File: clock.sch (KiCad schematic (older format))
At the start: 24 parts

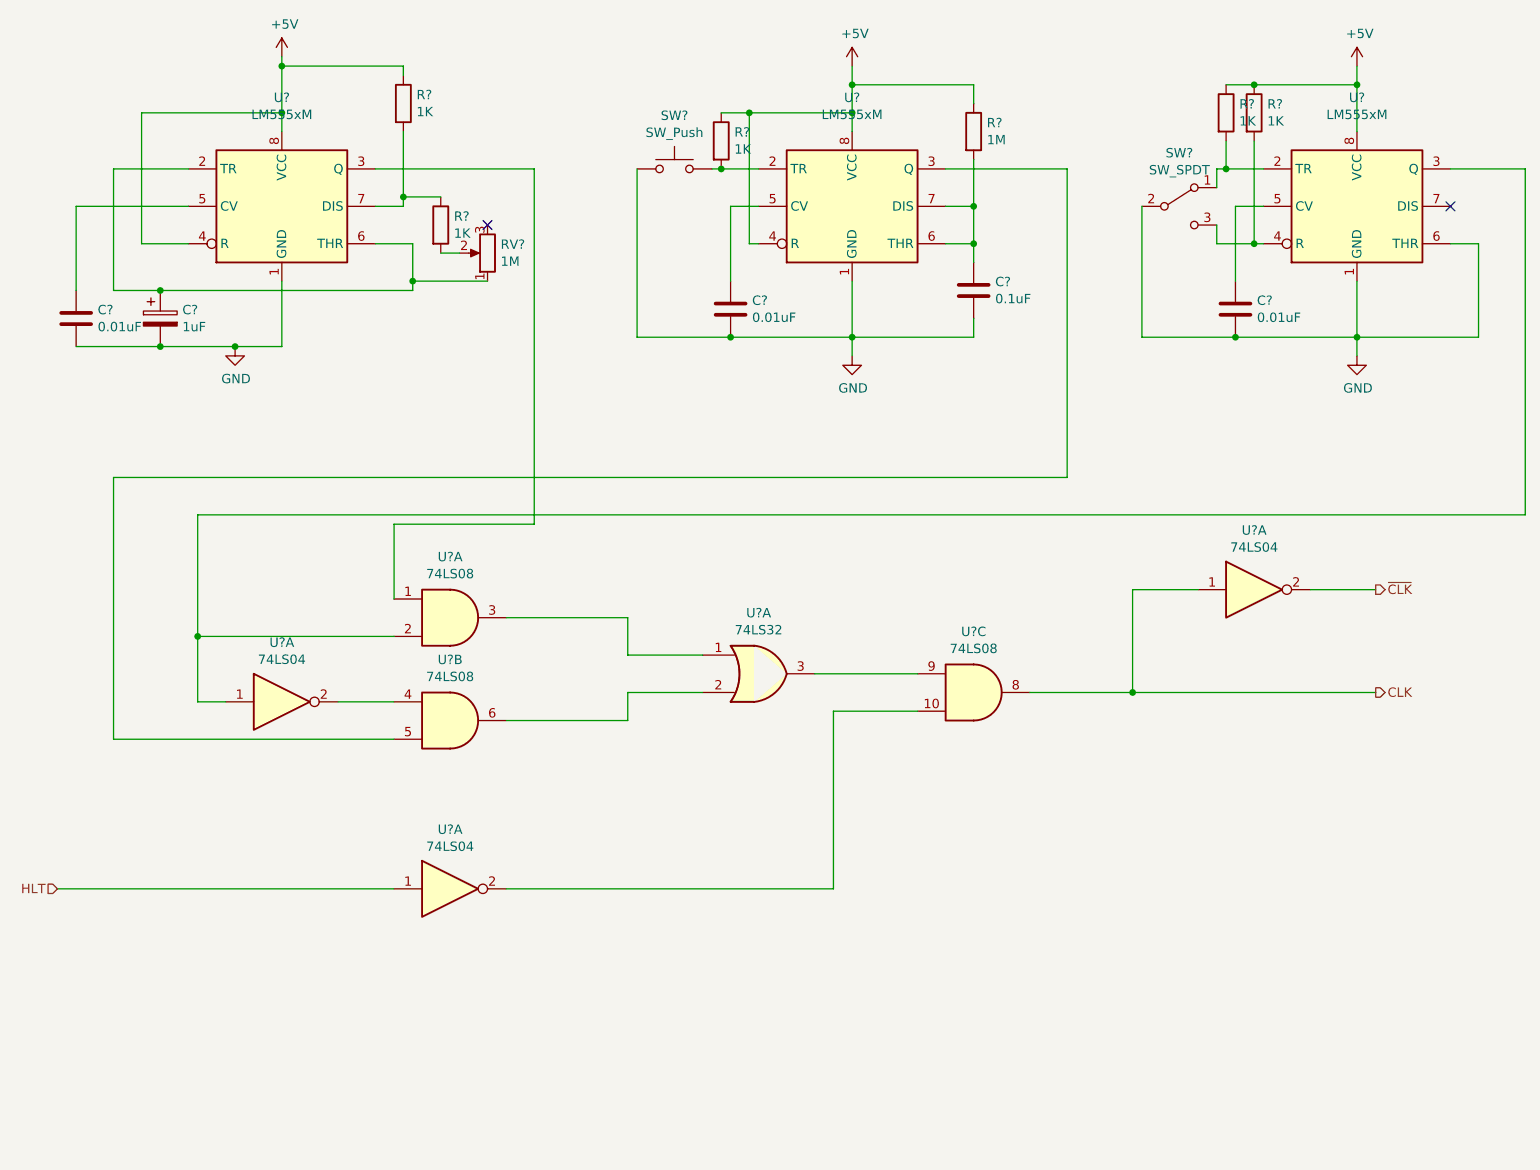
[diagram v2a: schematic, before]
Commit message: Added footprints
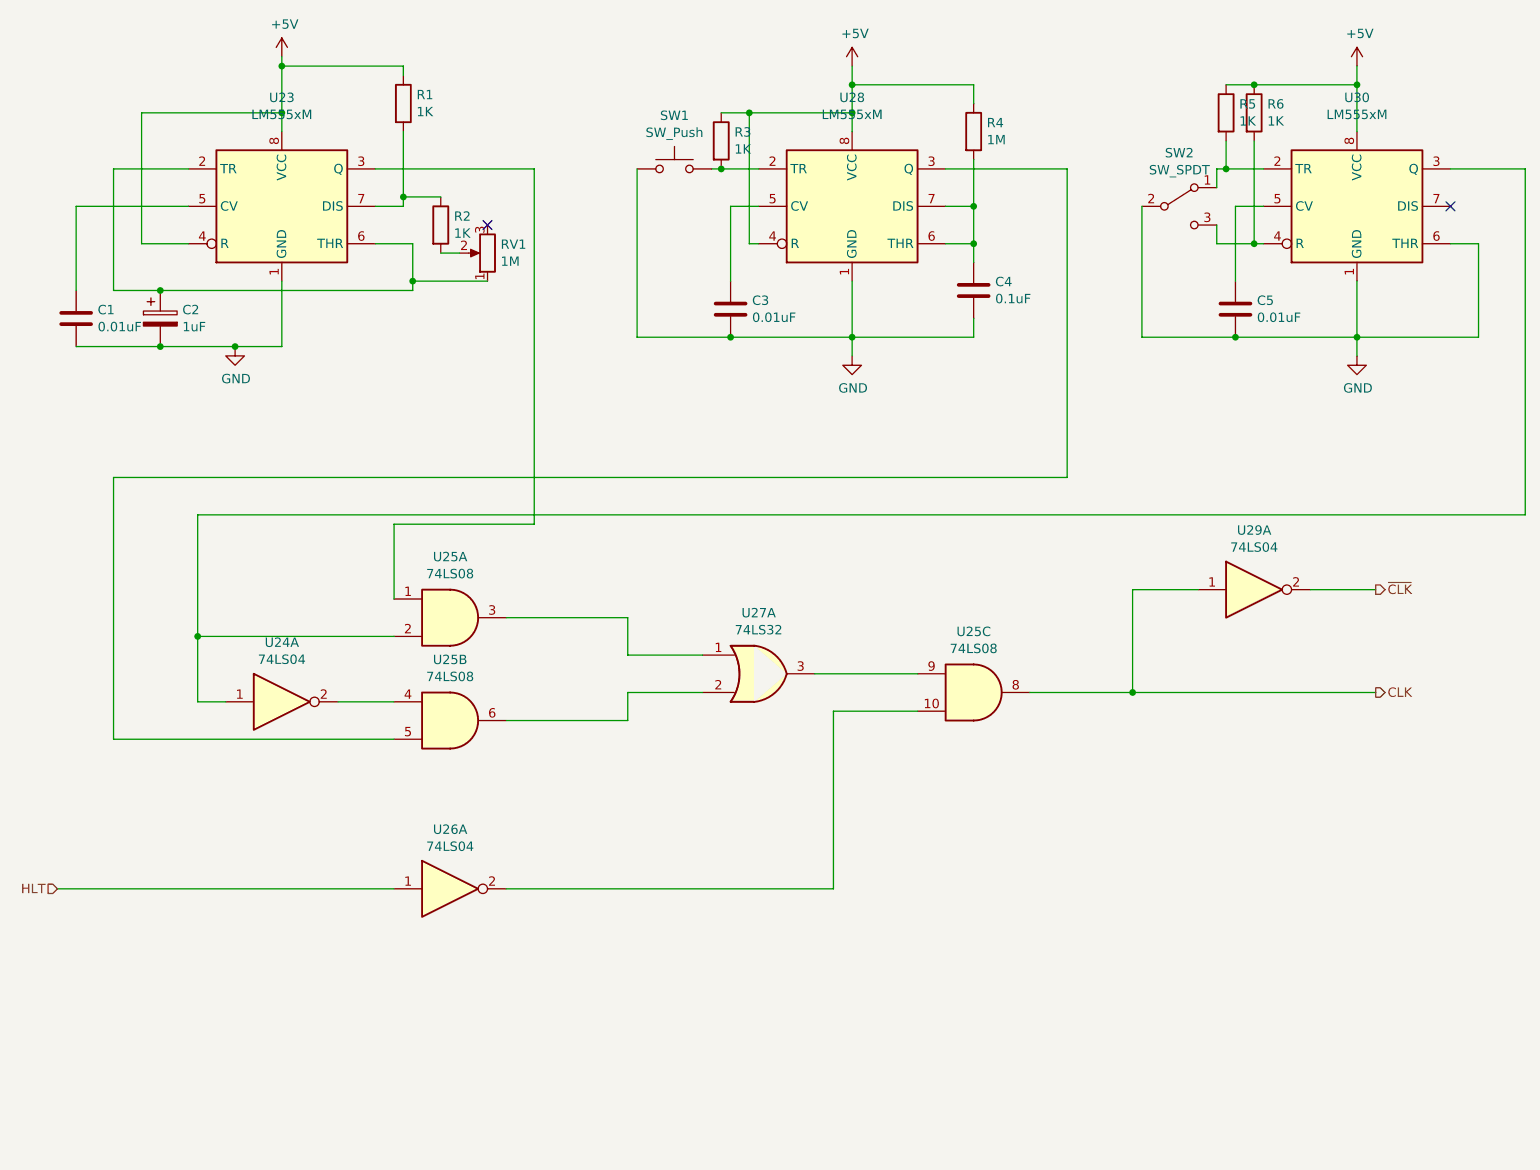
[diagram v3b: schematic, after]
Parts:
- C1, C2, C3, C4, C5: renamed from C?; footprint (none) -> Capacitor_THT:CP_Axial_L10.0mm_D4.5mm_P15.00mm_Horizontal
- R1, R2, R3, R4, R5, R6: renamed from R?; footprint (none) -> Resistor_THT:R_Axial_DIN0204_L3.6mm_D1.6mm_P7.62mm_Horizontal
- RV1: renamed from RV?; footprint (none) -> ROM:Potentiometer-5.5mm
- SW1: renamed from SW?; footprint (none) -> Button_Switch_THT:SW_PUSH-12mm
- SW2: renamed from SW?; footprint (none) -> ROM:DPDT-pushbutton
- U24, U25, U26, U27, U29: renamed from U?; footprint (none) -> Package_DIP:DIP-14_W7.62mm
- gave numbers to parts that had none: 3
